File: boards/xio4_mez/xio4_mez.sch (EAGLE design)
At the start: 89 parts, among them IC1 SN74LVC2G07DCKR, IC2 SN74LVC1G07MDCKREP, IC3 NL17SZ126XV5T2G, IC4 TPS2051BDBVR, Q1 SMMBT3904LT1G

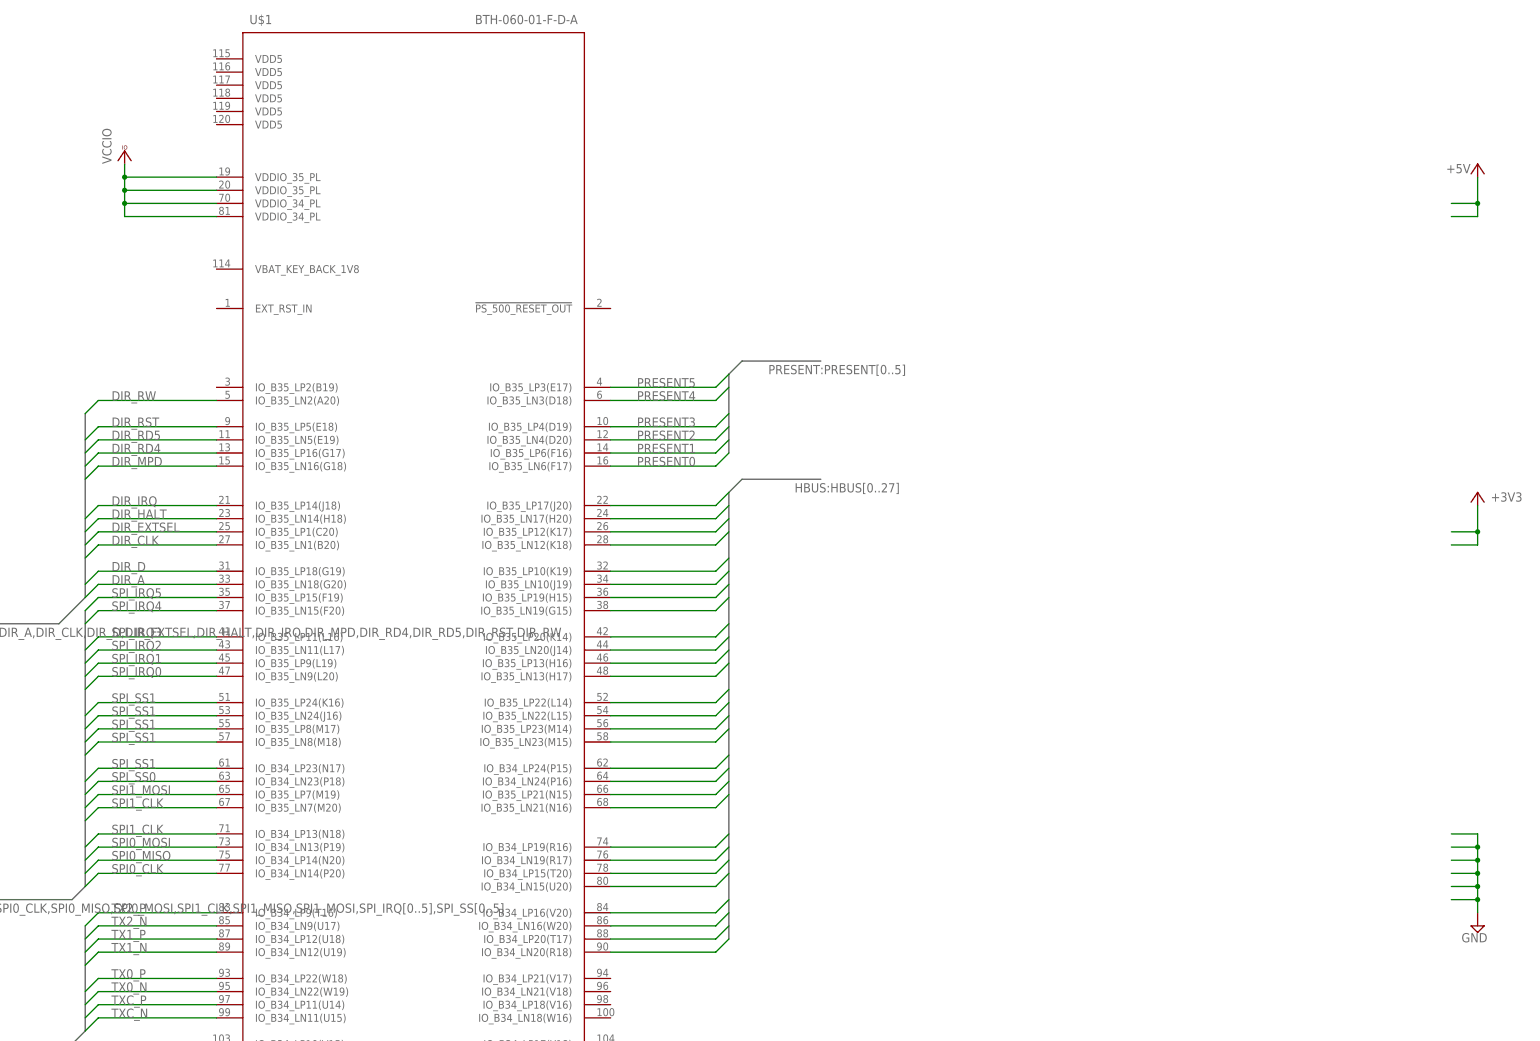
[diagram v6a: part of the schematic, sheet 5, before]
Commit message: Fully routed board
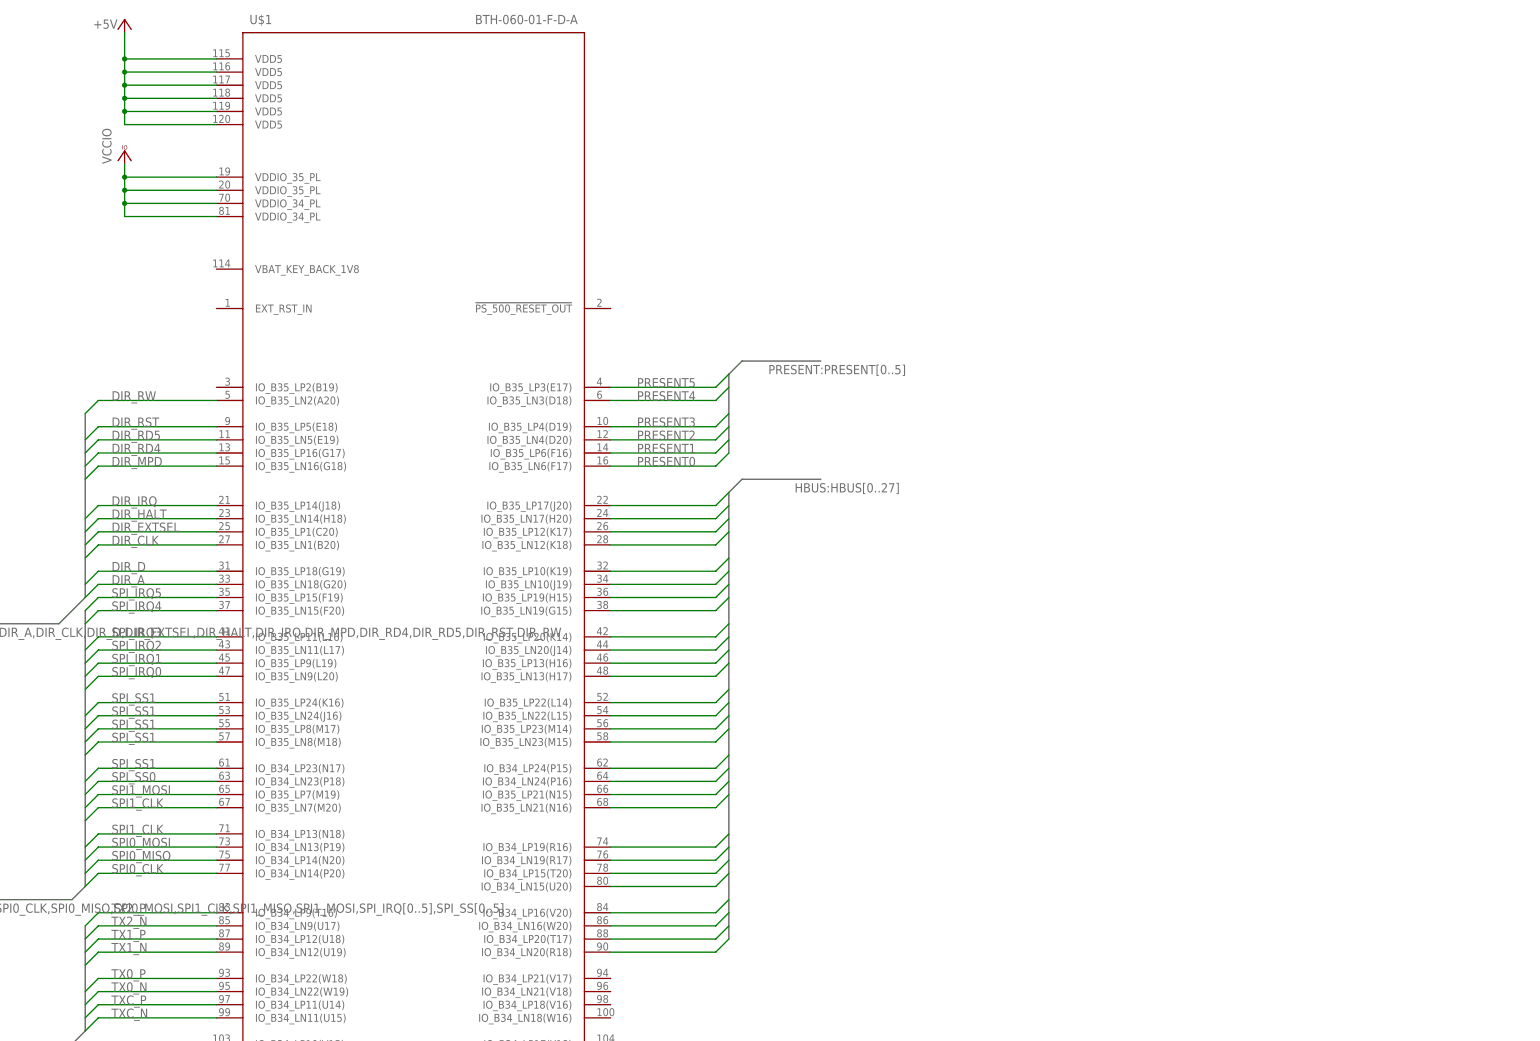
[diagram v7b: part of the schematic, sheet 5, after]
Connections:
- net +5V: now also U$1.VDD5@115, U$1.VDD5@116, U$1.VDD5@117, U$1.VDD5@118, U$1.VDD5@119, U$1.VDD5@120
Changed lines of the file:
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@@
 <setting verticaltext="up"/>
 </settings>
-<grid distance="0.1" unitdist="inch" unit="inch" style="lines" multiple="1" display="no" altdistance="0.01" altunitdist="inch" altunit="inch"/>
+<grid distance="0.1" unitdist="inch" unit="inch" style="lines" multiple="1" display="yes" altdistance="0.01" altunitdist="inch" altunit="inch"/>
 <layers>
 <layer number="1" name="Top" color="4" fill="1" visible="no" active="no"/>
@@
 <attribute name="USE" value="ERJ-1GNJ103C"/>
 </part>
-<part name="+3V20" library="supply1" library_urn="urn:adsk.eagle:library:371" deviceset="+3V3" device=""/>
 <part name="P+27" library="supply1" library_urn="urn:adsk.eagle:library:371" deviceset="+5V" device=""/>
-<part name="SUPPLY24" library="supply2" library_urn="urn:adsk.eagle:library:372" deviceset="GND" device=""/>
 <part name="CN1" library="microbuilder" deviceset="HDMI_MOLEX_47151-0001" device="">
 <attribute name="USE" value="047150001"/>
@@
 <attribute name="SHEET" x="164.465" y="-121.92" size="2.54" layer="94"/>
 </instance>
-<instance part="+3V20" gate="G$1" x="157.48" y="35.56" smashed="yes" rot="MR0">
-<attribute name="VALUE" x="160.02" y="35.56" size="1.778" layer="96" rot="MR180"/>
-</instance>
-<instance part="P+27" gate="1" x="157.48" y="99.06" smashed="yes" rot="MR0">
-<attribute name="VALUE" x="151.384" y="99.06" size="1.778" layer="96" rot="MR180"/>
-</instance>
-<instance part="SUPPLY24" gate="GND" x="157.48" y="-48.26" smashed="yes" rot="MR0">
-<attribute name="VALUE" x="159.385" y="-51.435" size="1.778" layer="96" rot="MR0"/>
+<instance part="P+27" gate="1" x="-104.14" y="127" smashed="yes" rot="MR0">
+<attribute name="VALUE" x="-110.236" y="127" size="1.778" layer="96" rot="MR180"/>
 </instance>
 <instance part="VCC1" gate="G$1" x="-104.14" y="101.6" smashed="yes">
@@
 </busses>
 <nets>
-<net name="+3V3" class="9">
-<segment>
-<pinref part="+3V20" gate="G$1" pin="+3V3"/>
-<wire x1="152.4" y1="27.94" x2="157.48" y2="27.94" width="0.1524" layer="91"/>
-<wire x1="157.48" y1="27.94" x2="157.48" y2="33.02" width="0.1524" layer="91"/>
-<wire x1="152.4" y1="25.4" x2="157.48" y2="25.4" width="0.1524" layer="91"/>
-<wire x1="157.48" y1="25.4" x2="157.48" y2="27.94" width="0.1524" layer="91"/>
-<junction x="157.48" y="27.94"/>
-</segment>
-</net>
-<net name="+5V" class="0">
-<segment>
-<pinref part="P+27" gate="1" pin="+5V"/>
-<wire x1="157.48" y1="96.52" x2="157.48" y2="91.44" width="0.1524" layer="91"/>
-<wire x1="157.48" y1="91.44" x2="152.4" y2="91.44" width="0.1524" layer="91"/>
-<wire x1="157.48" y1="91.44" x2="157.48" y2="88.9" width="0.1524" layer="91"/>
-<wire x1="157.48" y1="88.9" x2="152.4" y2="88.9" width="0.1524" layer="91"/>
-<junction x="157.48" y="91.44"/>
-</segment>
-</net>
 <net name="GND" class="0">
 <segment>
-<pinref part="SUPPLY24" gate="GND" pin="GND"/>
-<wire x1="157.48" y1="-45.72" x2="157.48" y2="-43.18" width="0.1524" layer="91"/>
-<wire x1="157.48" y1="-43.18" x2="152.4" y2="-43.18" width="0.1524" layer="91"/>
-<wire x1="157.48" y1="-43.18" x2="157.48" y2="-40.64" width="0.1524" layer="91"/>
-<wire x1="157.48" y1="-40.64" x2="152.4" y2="-40.64" width="0.1524" layer="91"/>
-<junction x="157.48" y="-43.18"/>
-<wire x1="157.48" y1="-40.64" x2="157.48" y2="-38.1" width="0.1524" layer="91"/>
-<junction x="157.48" y="-40.64"/>
-<wire x1="157.48" y1="-38.1" x2="152.4" y2="-38.1" width="0.1524" layer="91"/>
-<wire x1="157.48" y1="-38.1" x2="157.48" y2="-35.56" width="0.1524" layer="91"/>
-<wire x1="157.48" y1="-35.56" x2="152.4" y2="-35.56" width="0.1524" layer="91"/>
-<junction x="157.48" y="-38.1"/>
-<wire x1="157.48" y1="-35.56" x2="157.48" y2="-33.02" width="0.1524" layer="91"/>
-<wire x1="157.48" y1="-33.02" x2="152.4" y2="-33.02" width="0.1524" layer="91"/>
-<junction x="157.48" y="-35.56"/>
-<wire x1="157.48" y1="-33.02" x2="157.48" y2="-30.48" width="0.1524" layer="91"/>
-<wire x1="157.48" y1="-30.48" x2="152.4" y2="-30.48" width="0.1524" layer="91"/>
-<junction x="157.48" y="-33.02"/>
-</segment>
-<segment>
 <pinref part="U$1" gate="G$1" pin="GND@113"/>
 <pinref part="SUPPLY31" gate="GND" pin="GND"/>
@@
 </segment>
 </net>
+<net name="+5V" class="0">
+<segment>
+<pinref part="P+27" gate="1" pin="+5V"/>
+<wire x1="-104.14" y1="124.46" x2="-104.14" y2="119.38" width="0.1524" layer="91"/>
+<pinref part="U$1" gate="G$1" pin="VDD5@120"/>
+<wire x1="-104.14" y1="119.38" x2="-104.14" y2="116.84" width="0.1524" layer="91"/>
+<wire x1="-104.14" y1="116.84" x2="-104.14" y2="114.3" width="0.1524" layer="91"/>
+<wire x1="-104.14" y1="114.3" x2="-104.14" y2="111.76" width="0.1524" layer="91"/>
+<wire x1="-104.14" y1="111.76" x2="-104.14" y2="109.22" width="0.1524" layer="91"/>
+<wire x1="-104.14" y1="109.22" x2="-104.14" y2="106.68" width="0.1524" layer="91"/>
+<wire x1="-104.14" y1="106.68" x2="-86.36" y2="106.68" width="0.1524" layer="91"/>
+<pinref part="U$1" gate="G$1" pin="VDD5@119"/>
+<wire x1="-86.36" y1="109.22" x2="-104.14" y2="109.22" width="0.1524" layer="91"/>
+<junction x="-104.14" y="109.22"/>
+<pinref part="U$1" gate="G$1" pin="VDD5@118"/>
+<wire x1="-86.36" y1="111.76" x2="-104.14" y2="111.76" width="0.1524" layer="91"/>
+<junction x="-104.14" y="111.76"/>
+<pinref part="U$1" gate="G$1" pin="VDD5@117"/>
+<wire x1="-86.36" y1="114.3" x2="-104.14" y2="114.3" width="0.1524" layer="91"/>
+<junction x="-104.14" y="114.3"/>
+<pinref part="U$1" gate="G$1" pin="VDD5@116"/>
+<wire x1="-86.36" y1="116.84" x2="-104.14" y2="116.84" width="0.1524" layer="91"/>
+<junction x="-104.14" y="116.84"/>
+<pinref part="U$1" gate="G$1" pin="VDD5@115"/>
+<wire x1="-86.36" y1="119.38" x2="-104.14" y2="119.38" width="0.1524" layer="91"/>
+<junction x="-104.14" y="119.38"/>
+</segment>
+</net>

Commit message: Latest routed board
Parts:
- CN1: USE 047150001 -> 0471510001
- D2: USE (none) -> 150080RS75000
- IC1: USE (none) -> SN74LVC2G07DCKR
- IC2: USE (none) -> SN74LVC1G07MDCKREP
- IC3: USE (none) -> NL17SZ126XV5T2G
- IC4: USE (none) -> TPS2051BDBVR
- JP1, JP2, JP3: USE (none) -> NPTC152KFMS-RC
- Q1: USE (none) -> SMMBT3904LT1G
- R1, R11, R12, R14, R6, R7, R8, R9: USE (none) -> RC0201FR-0749R9L
- R15: USE (none) -> RC0201FR-0727KL
- R16, R17: USE (none) -> RC0201JR-071K5L
- R18, R20: USE (none) -> RC0201FR-074K7L
- R23, R27: USE (none) -> RC0201FR-07100KL
- R24, R28, R30: USE (none) -> RC0201FR-071KL
- R29, R31, R32: USE (none) -> ERJ-1GNJ103C
- R33: USE (none) -> RC0201JR-07820RL
- U$1: USE (none) -> BTH-060-01-F-D-A
